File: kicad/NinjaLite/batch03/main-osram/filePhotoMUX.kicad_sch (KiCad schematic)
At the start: 34 parts, among them U19 CD74HC4067M96

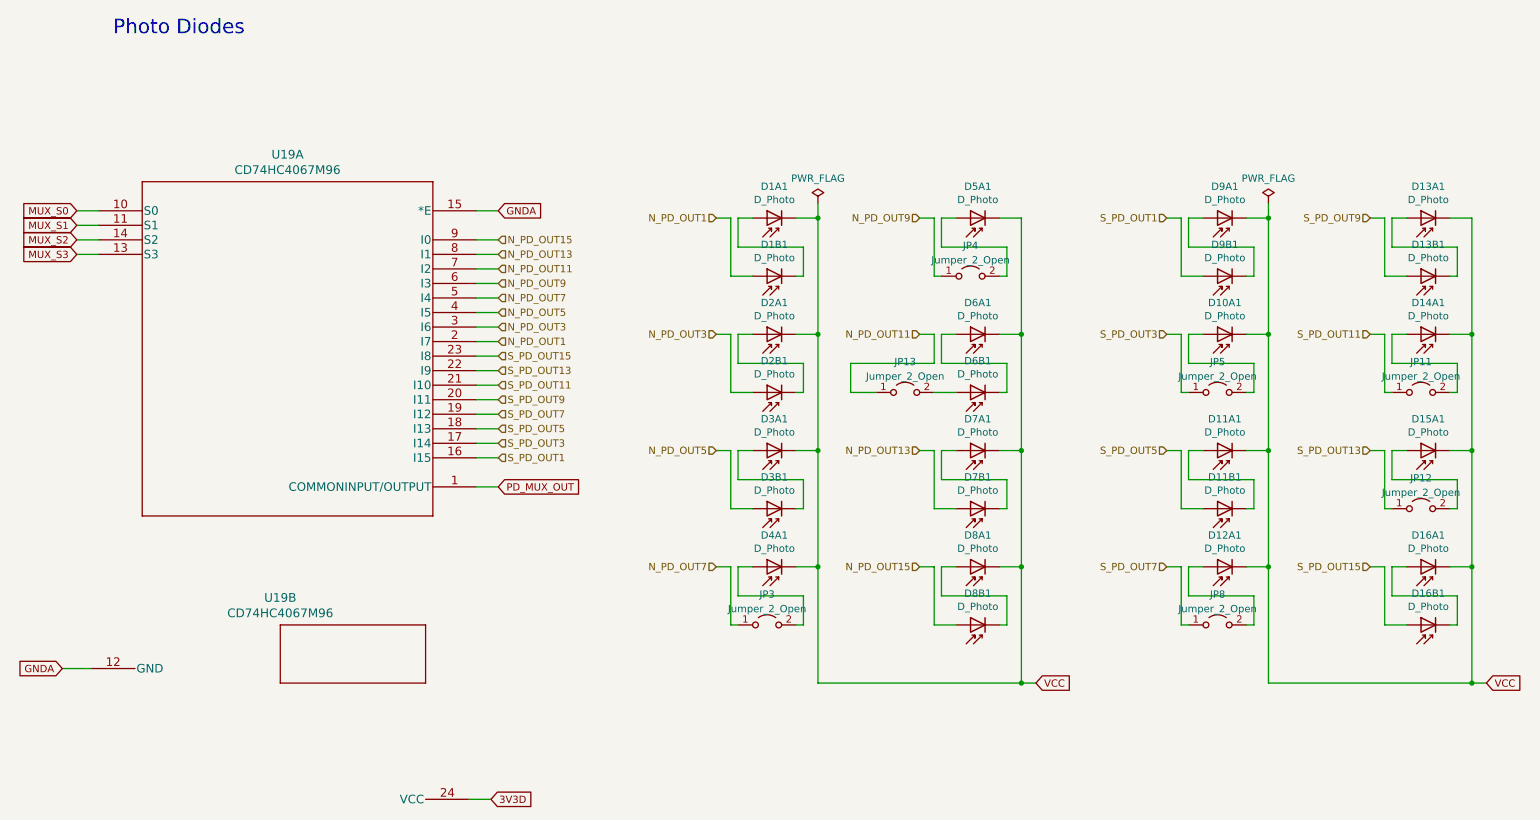
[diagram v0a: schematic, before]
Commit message: add pads below all pds
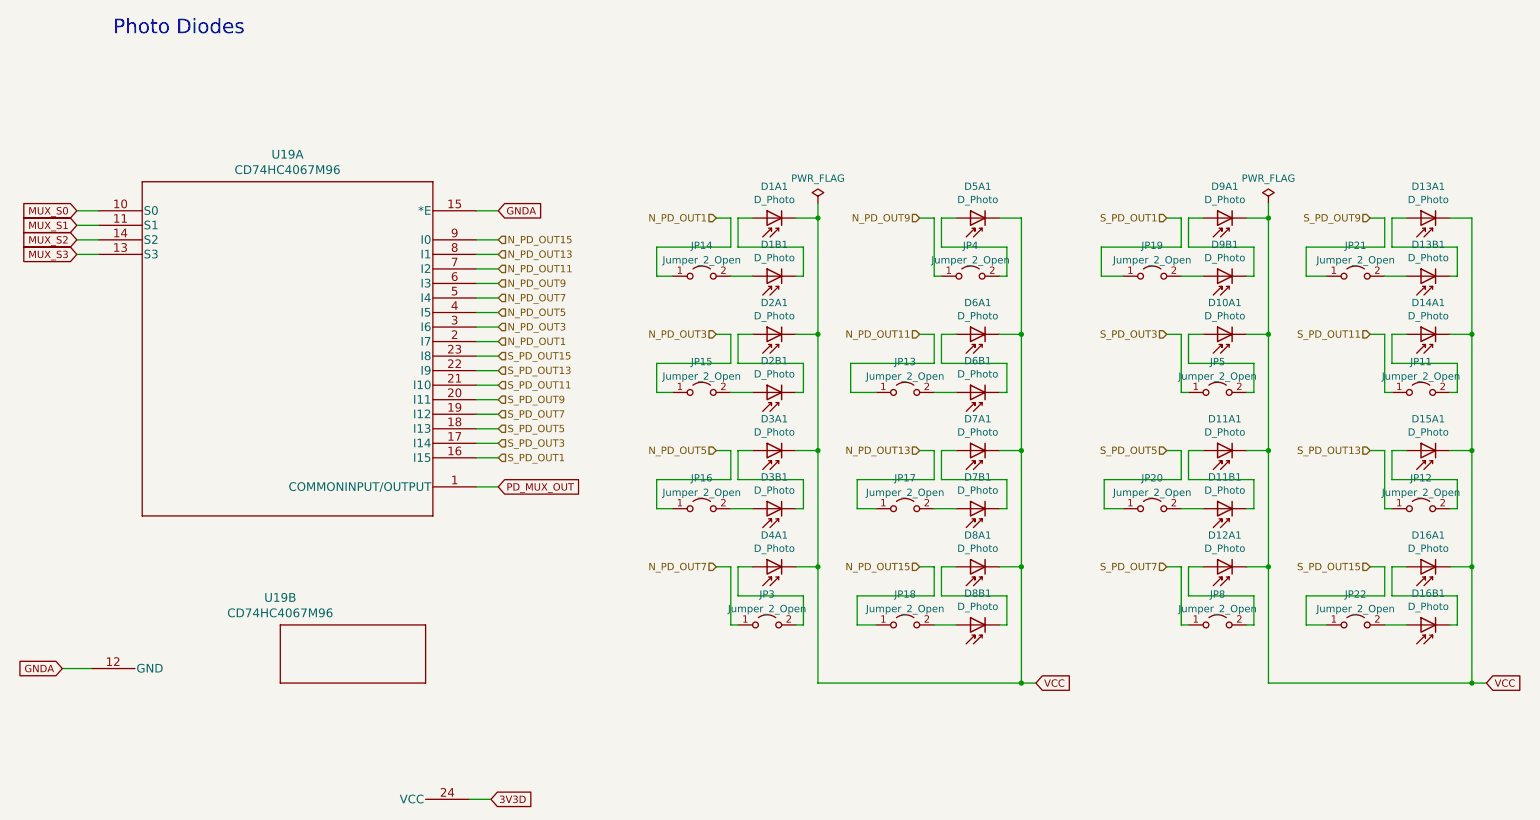
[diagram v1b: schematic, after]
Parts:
- added JP14, JP15, JP16, JP17, JP18, JP19, JP20, JP21, JP22: Jumper_2_Open, Jumper:SolderJumper-2_P1.3mm_Open_RoundedPad1.0x1.5mm, symbol Jumper:Jumper_2_Open
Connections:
- net N_PD_OUT1: now also JP14.1 (A); no longer D1B1.2 (A)
- net N_PD_OUT13: now also JP17.1 (A); no longer D7B1.2 (A)
- net N_PD_OUT15: now also JP18.1 (A); no longer D8B1.2 (A)
- net N_PD_OUT3: now also JP15.1 (A); no longer D2B1.2 (A)
- net N_PD_OUT5: now also JP16.1 (A); no longer D3B1.2 (A)
- net S_PD_OUT1: now also JP19.1 (A); no longer D9B1.2 (A)
- net S_PD_OUT15: now also JP22.1 (A); no longer D16B1.2 (A)
- net S_PD_OUT5: now also JP20.1 (A); no longer D11B1.2 (A)
- net S_PD_OUT9: now also JP21.1 (A); no longer D13B1.2 (A)
- new net: D13B1.2 (A), JP21.2 (B)
- new net: D2B1.2 (A), JP15.2 (B)
- new net: D3B1.2 (A), JP16.2 (B)
- new net: D7B1.2 (A), JP17.2 (B)
- new net: D16B1.2 (A), JP22.2 (B)
- new net: D9B1.2 (A), JP19.2 (B)
- new net: D8B1.2 (A), JP18.2 (B)
- new net: D1B1.2 (A), JP14.2 (B)
- new net: D11B1.2 (A), JP20.2 (B)
